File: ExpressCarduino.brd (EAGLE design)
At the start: 38.8 x 27.7 mm, 14 parts, among them IC1 MCP23017ML, U1 AP3012

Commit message: I keep tweaking the board...
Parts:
- removed U$2: SN74LV4051A, HokieGeek:TSSOP16
- added IC2: SN74LV4051A, HokieGeek:TSSOP16
- moved IC1 0.48 mm to (6.76, 17.0)
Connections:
- net GND: now also IC2.7, IC2.8; no longer U$2.7, U$2.8
- net MUX_A: now also IC2.11; no longer U$2.11
- net MUX_B: now also IC2.10; no longer U$2.10
- net MUX_C: now also IC2.9; no longer U$2.9
- net MUX_COM: now also IC2.3; no longer U$2.3
- net N$19: now also IC2.13; no longer U$2.13
- net N$20: now also IC2.14; no longer U$2.14
- net N$21: now also IC2.15; no longer U$2.15
- net N$22: now also IC2.12; no longer U$2.12
- net N$23: now also IC2.1; no longer U$2.1
- net N$24: now also IC2.5; no longer U$2.5
- net N$25: now also IC2.2; no longer U$2.2
- net N$26: now also IC2.4; no longer U$2.4
- net VCC: now also IC2.16; no longer U$2.16
- net VUSB: now also IC2.6; no longer U$2.6
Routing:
- net 9V: track 20.2 -> 37.5 mm
- net N$21: track 29.7 -> 43.5 mm
- net N$8: track 31.2 -> 19.7 mm, vias 4 -> 2
- net N$2: track 29.8 -> 38.8 mm, vias 0 -> 3
- net USBD-: track 20.7 -> 13.8 mm
- net VUSB: track 36.2 -> 43.1 mm
- net GND_USB: track 43.1 -> 47.6 mm, vias 5 -> 4
- net N$22: track 28.3 -> 24.7 mm, vias 0 -> 1
- net N$1: track 16.4 -> 19.4 mm, vias 0 -> 5
- net USBD+: track 18.8 -> 15.8 mm
- net N$23: track 27.9 -> 30.8 mm
- net N$19: track 35.9 -> 33.2 mm
- net MUX_A: track 9.88 -> 7.33 mm, vias 2 -> 0
- net N$5: track 24.4 -> 26.9 mm
- net MUX_COM: track 13.9 -> 11.9 mm
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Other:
- outline, holes or cut-outs redrawn
- board text added: "20151111"
- board text added: "HokieGeek"
- board text removed: "20151110"

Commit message: More tweaks
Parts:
- moved R2 5.46 mm to (4.33, 12.0), turned to 180 degrees
- moved C2 4.94 mm to (4.24, 16.1), turned to 270 degrees
- moved C1 3.05 mm to (14.5, 4.08), turned to 180 degrees
- moved ADC 2.40 mm to (34.5, 25.6)
- moved GPIO 2.39 mm to (34.4, 21.6)
- moved IC1 2.16 mm to (8.91, 17.2)
- moved JP1 1.80 mm to (15.1, 19.2)
- moved R1 1.05 mm to (14.5, 1.31), turned to 0 degrees
- moved U1 0.59 mm to (4.23, 7.89)
- moved D1 0.28 mm to (11.1, 2.89)
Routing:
- net 9V: track 37.5 -> 17.8 mm
- net N$21: track 43.5 -> 25.1 mm
- net GND_USB: track 47.6 -> 30.6 mm, vias 4 -> 2
- net N$23: track 30.8 -> 13.9 mm, vias 2 -> 0
- net N$2: track 38.8 -> 25.4 mm, vias 3 -> 1
- net N$4: track 29.0 -> 39.5 mm, vias 0 -> 1
- net N$25: track 14.0 -> 8.55 mm, vias 1 -> 0
- net N$8: track 19.7 -> 14.5 mm, vias 2 -> 1
- net GND: track 45.9 -> 50.8 mm, vias 5 -> 3
- net N$6: track 23.2 -> 18.4 mm
- net N$20: track 30.9 -> 35.5 mm, vias 0 -> 1
- net N$5: track 26.9 -> 22.4 mm
- net N$7: track 19.1 -> 14.7 mm, vias 1 -> 0
- net N$1: track 19.4 -> 23.5 mm, vias 5 -> 2
- net N$10: track 12.8 -> 8.86 mm
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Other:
- board size 38.8 x 27.7 mm -> 36.5 x 27.7 mm

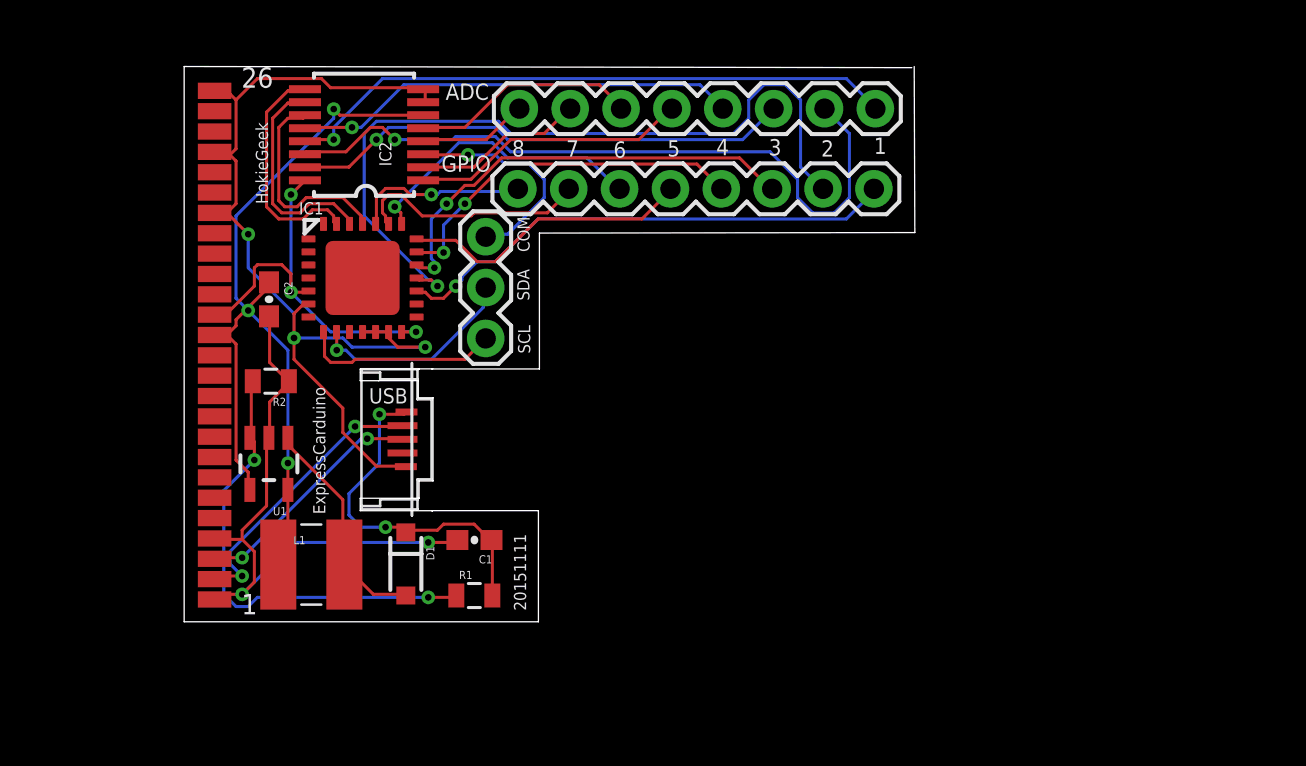
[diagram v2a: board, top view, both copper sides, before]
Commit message: Added power supply pins based on #10
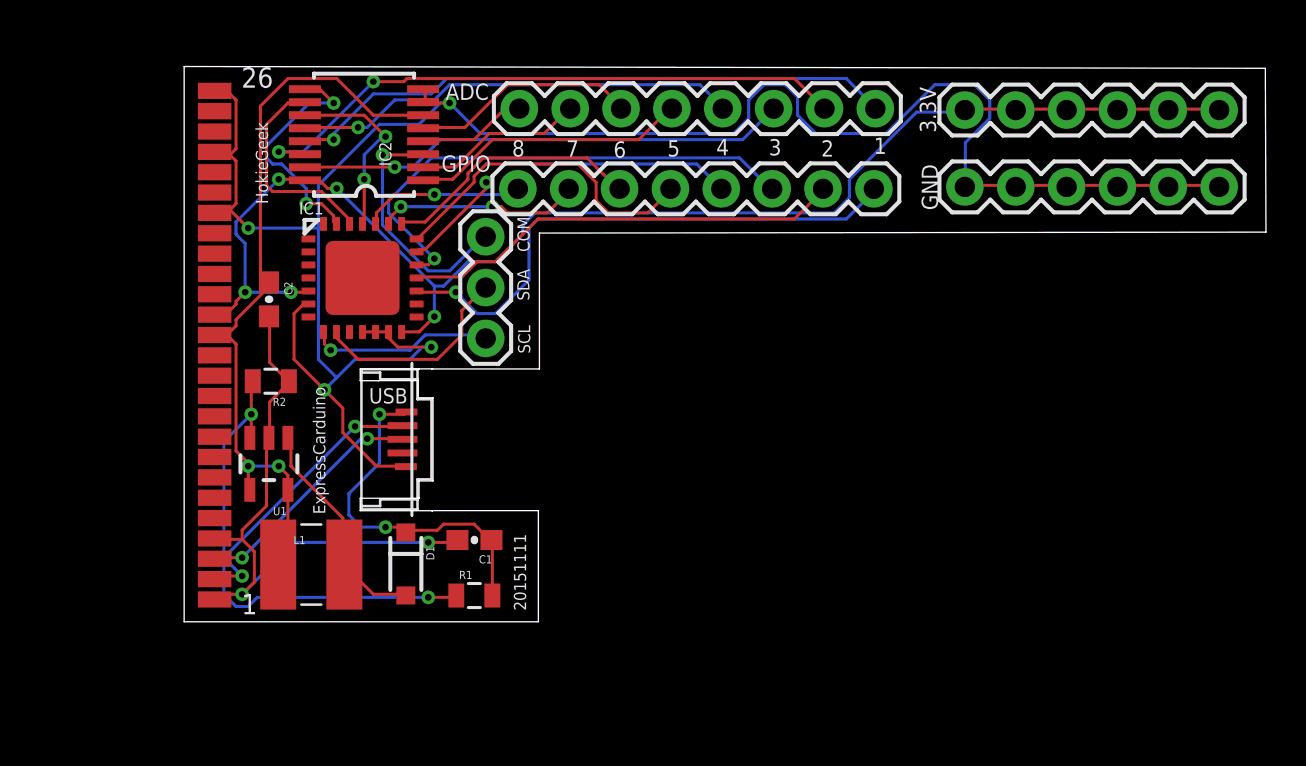
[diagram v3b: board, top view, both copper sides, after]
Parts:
- added 3.3V, GND: (no value), SparkFun-Connectors:1X06
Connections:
- net GND: now also GND.1, GND.2, GND.3, GND.4, GND.5, GND.6
- net VCC: now also 3.3V.1, 3.3V.2, 3.3V.3, 3.3V.4, 3.3V.5, 3.3V.6
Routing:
- net GND: track 50.8 -> 107.4 mm, vias 3 -> 4
- net VCC: track 21.1 -> 69.3 mm, vias 3 -> 5
- net N$4: track 39.5 -> 22.2 mm, vias 1 -> 0
- net VUSB: track 43.8 -> 38.2 mm, vias 3 -> 2
- net N$20: track 35.5 -> 30.8 mm, vias 1 -> 2
- net N$5: track 22.4 -> 25.5 mm, vias 2 -> 1
- net N$2: track 25.4 -> 27.5 mm
- net N$7: track 14.7 -> 16.5 mm
- net N$9: track 11.8 -> 10.2 mm, vias 0 -> 2
- net N$8: track 14.5 -> 13.1 mm, vias 1 -> 0
- net MUX_COM: track 11.3 -> 12.3 mm
- net MUX_A: track 10.5 -> 9.39 mm, vias 0 -> 2
- net N$1: track 23.5 -> 24.5 mm
- net GPIO_SCL: track 9.89 -> 9.17 mm, vias 0 -> 1
- net N$10: track 8.86 -> 8.16 mm
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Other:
- board size 36.5 x 27.7 mm -> 54 x 27.7 mm

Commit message: Trying things out
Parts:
- added IC3: MCP23008, HokieGeek:QFN-20-0.4MM-V2
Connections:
- net GND: now also IC3.17
- net VCC: now also IC3.18
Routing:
- net GND: track 107.4 -> 0.00 mm, vias 4 -> 0
- net VCC: track 69.3 -> 0.00 mm, vias 5 -> 0
- net VUSB: track 38.2 -> 0.00 mm, vias 2 -> 0
- net N$20: track 30.8 -> 0.00 mm, vias 2 -> 0
- net GND_USB: track 30.6 -> 0.00 mm, vias 2 -> 0
- net N$19: track 30.6 -> 0.00 mm, vias 1 -> 0
- net N$2: track 27.5 -> 0.00 mm, vias 1 -> 0
- net N$5: track 25.5 -> 0.00 mm, vias 1 -> 0
- net N$21: track 24.6 -> 0.00 mm, vias 1 -> 0
- net N$1: track 24.5 -> 0.00 mm, vias 2 -> 0
- net N$22: track 22.3 -> 0.00 mm, vias 1 -> 0
- net N$4: track 22.2 -> 0.00 mm
- net 9V: track 17.8 -> 0.00 mm, vias 2 -> 0
- net N$6: track 17.7 -> 0.00 mm, vias 1 -> 0
- net N$7: track 16.5 -> 0.00 mm
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
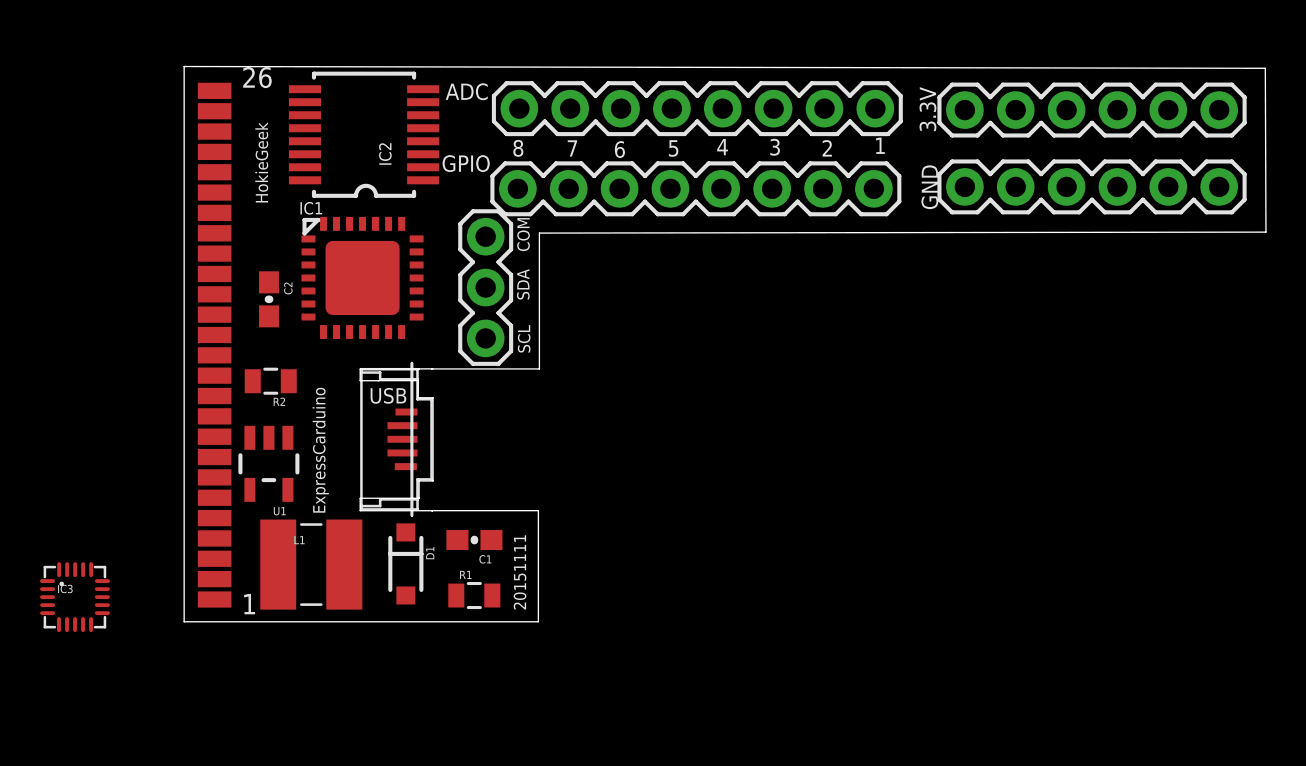
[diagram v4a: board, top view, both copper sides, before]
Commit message: Modified current schematic to remove potential nogo and added "basic" board
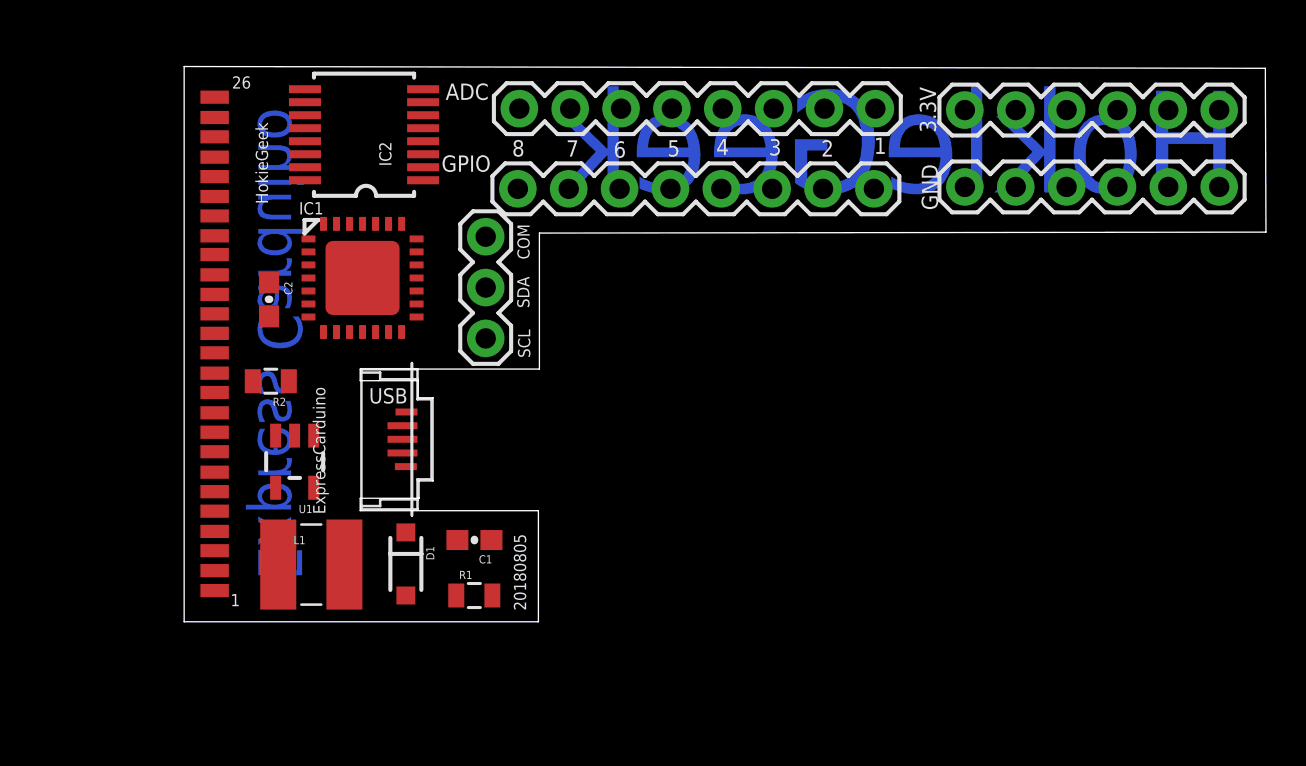
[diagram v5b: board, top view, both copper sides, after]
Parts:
- removed IC3: MCP23008, HokieGeek:QFN-20-0.4MM-V2
- IC2: value SN74LV4051A -> SN74LV4051APWR
- moved U1 1.29 mm to (5.52, 7.99)
- moved U$1 0.48 mm to (1.59, 14.5)
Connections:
- net GND: no longer IC3.17
- net VCC: no longer IC3.18
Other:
- outline, holes or cut-outs redrawn
- board text added: "20180805"
- board text added: "Express Carduino"
- board text removed: "20151111"
